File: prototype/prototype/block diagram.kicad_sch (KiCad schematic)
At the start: 30 parts, among them J1 Conn_01x06_Pin, Q2 NMOS, Q3 NMOS, Q4 NMOS, U10 AMS1117-3.3, U11 ESP32-WROOM-32E, U8 CI121S021 [adc], U9 MQ-4M

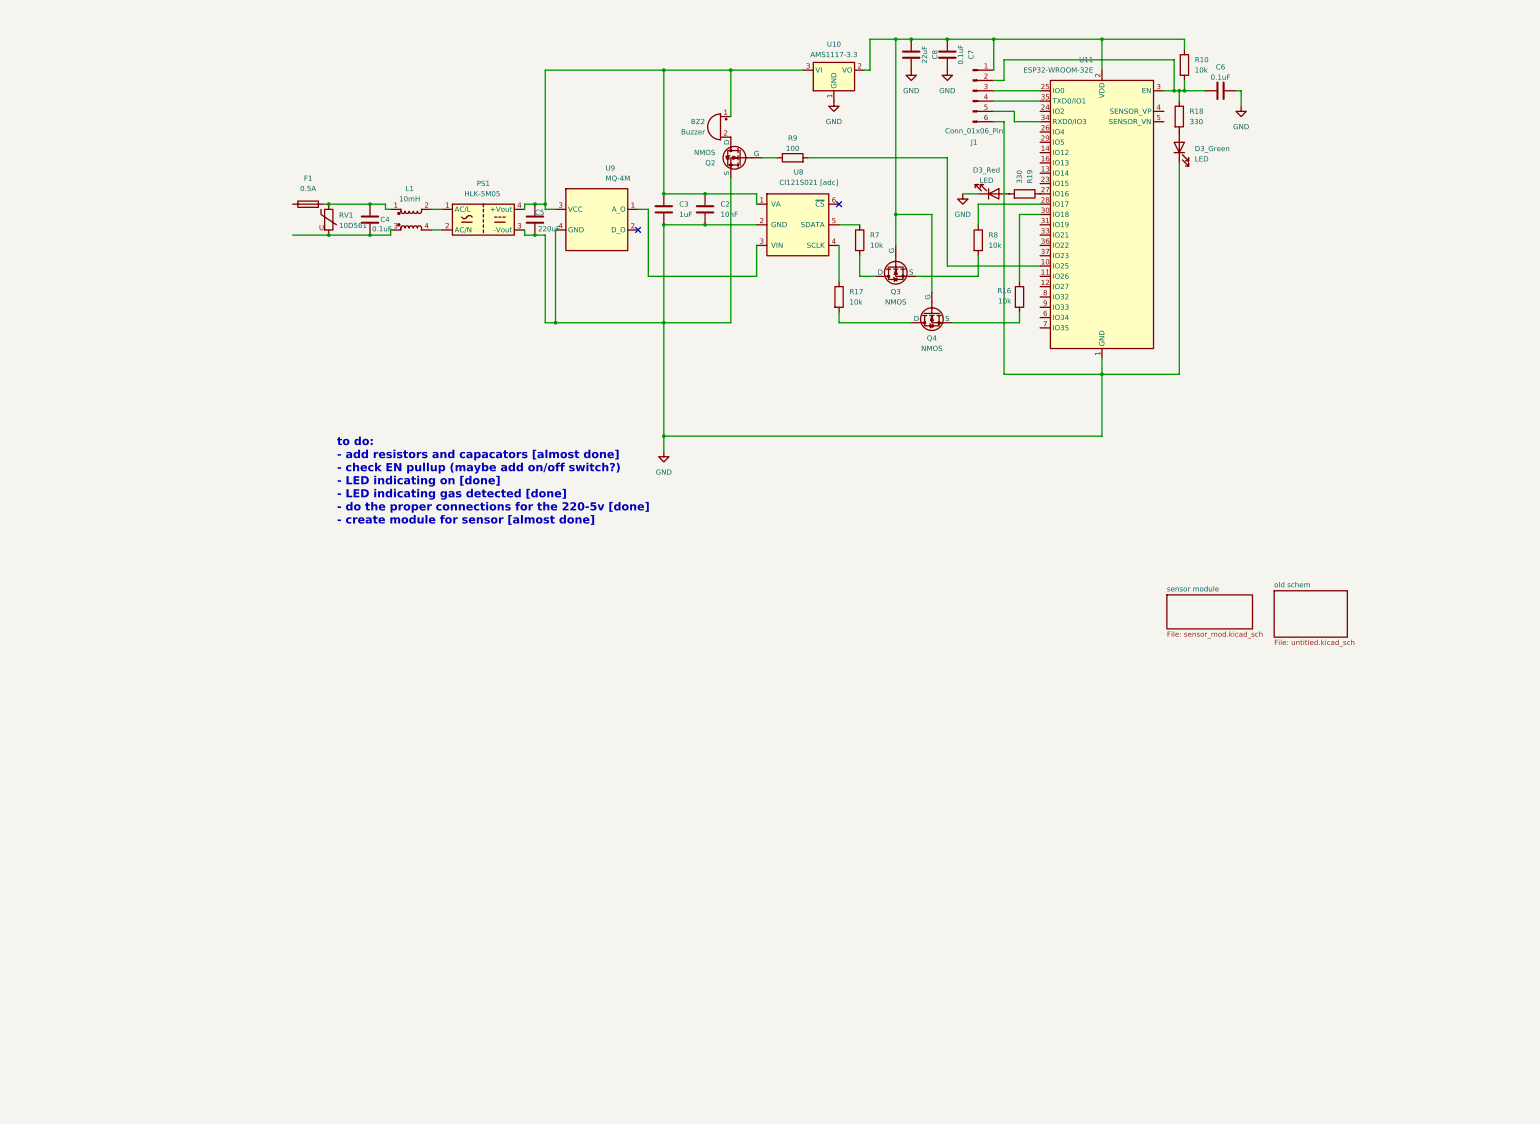
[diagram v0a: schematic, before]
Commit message: cleaning up schematic of prototype
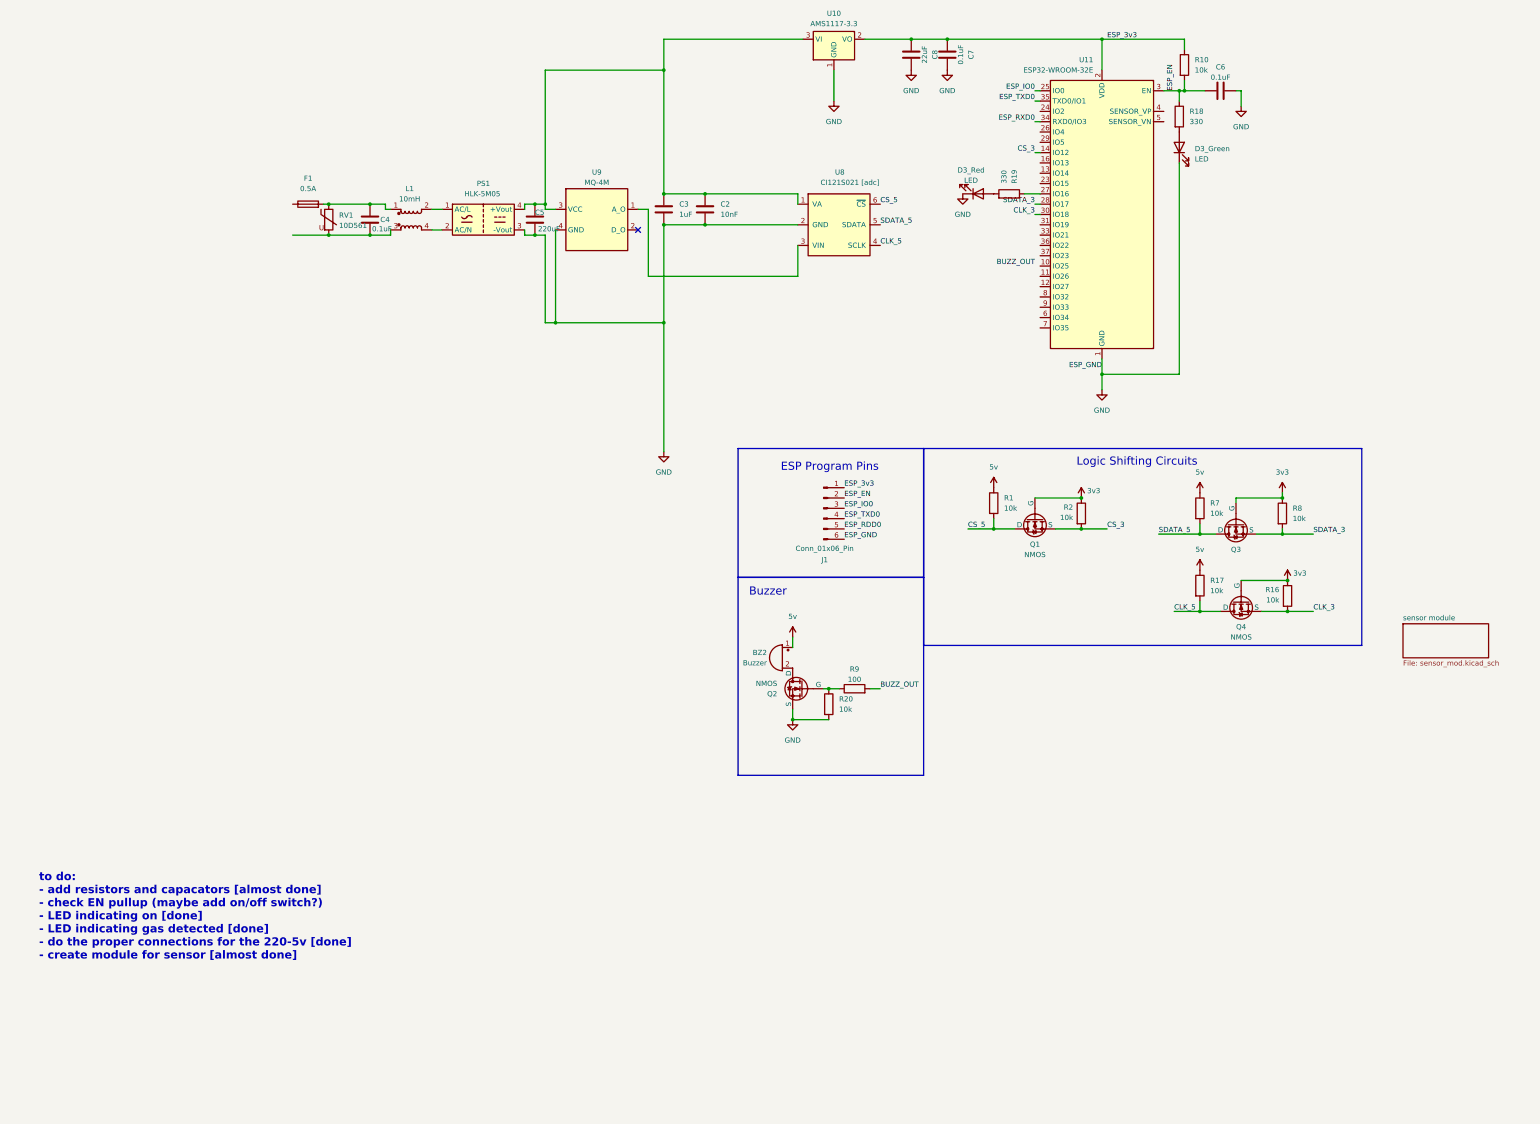
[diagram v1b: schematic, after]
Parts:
- added Q1: NMOS, symbol Simulation_SPICE:NMOS
- added R1, R2, R20: 10k, symbol Device:R
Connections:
- net GND: now also R20.2
- net 3v3: now reaches R16.1
- net 3v3: now also Q3.2 (G), Q4.2 (G), R8.1, Q1.2 (G), R2.1; no longer U11.30 (IO18)
- net CLK_3: now reaches Q4.3 (S), R16.2
- net CLK_3: now also U11.30 (IO18)
- net CLK_5: now reaches Q4.1 (D), R17.2
- net CLK_5: now also U8.4 (SCLK)
- net ESP_3v3: now reaches C7.1, C8.1, J1.1 (Pin_1), R10.1, U10.2 (VO), U11.2 (VDD)
- net ESP_3v3: no longer Q3.2 (G), Q4.2 (G)
- net at Q2.2 (G), R9.1: now also R20.1
- net at U11.10 (IO25): no longer R9.2
- net at C2.1, C3.1, C5.1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: no longer BZ2.1 (+)
- net 5v: now reaches R7.1
- net 5v: now also BZ2.1 (+), R17.1, R1.1; no longer U8.5 (SDATA)
- net SDATA_5: now reaches Q3.1 (D), R7.2
- net SDATA_5: now also U8.5 (SDATA)
- net SDATA_3: now reaches Q3.3 (S), R8.2
- net SDATA_3: now also U11.28 (IO17)
- net ESP_EN: now reaches C6.1, J1.2 (Pin_2), R10.2, R18.1, U11.3 (EN)
- net CS_5: now reaches U8.6 (~{CS})
- net CS_5: now also Q1.1 (D), R1.2
- net CS_3: now reaches U11.14 (IO12)
- net CS_3: now also Q1.3 (S), R2.2
- net ESP_IO0: now reaches J1.3 (Pin_3), U11.25 (IO0)
- net ESP_RDD0: now reaches J1.5 (Pin_5)
- net ESP_RDD0: no longer U11.34 (RXD0/IO3)
- net ESP_TXD0: now reaches J1.4 (Pin_4), U11.35 (TXD0/IO1)
- new net BUZZ_OUT: R9.2
- new net ESP_RXD0: U11.34 (RXD0/IO3)
- no-connect marks 2 -> 1
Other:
- removed sheet old schem
- note added: "Buzzer"
- note added: "ESP Program Pins"
- note added: "Logic Shifting Circuits"
- moved on the sheet: BZ2, D3_Red, J1, Q2, Q3, Q4, R16, R17, R19, R7, R8, R9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

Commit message: cleaning up schematic of prototype complete
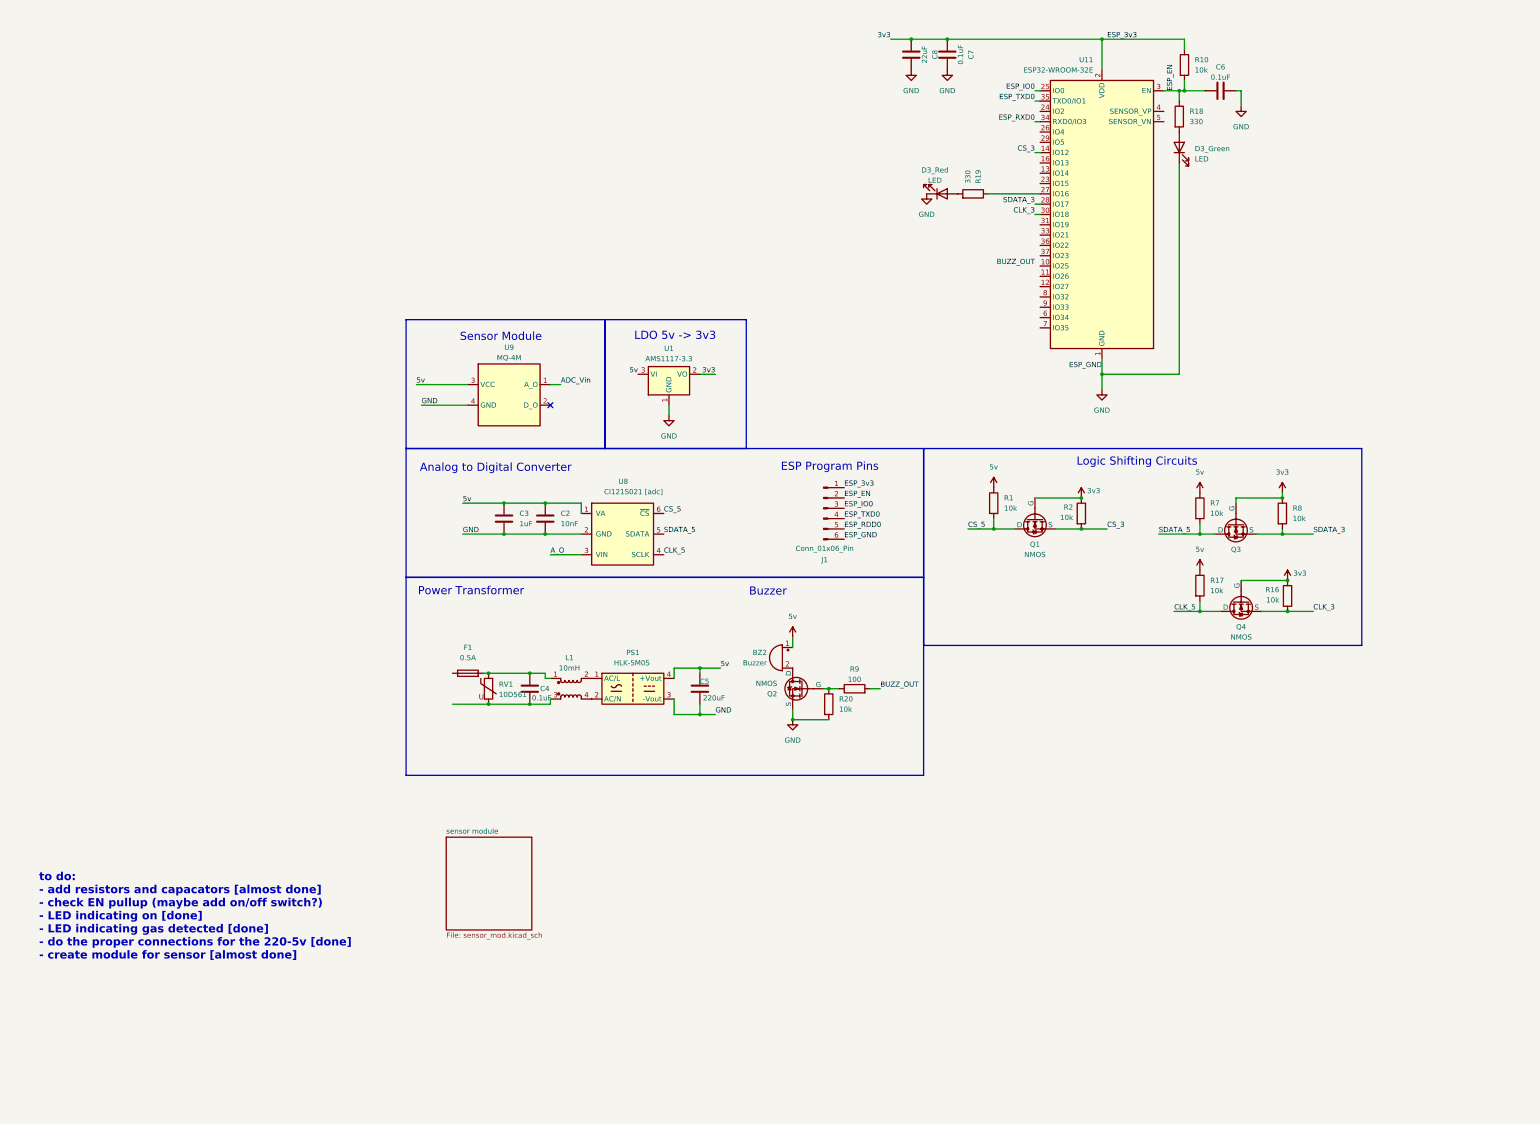
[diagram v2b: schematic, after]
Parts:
- removed U10: AMS1117-3.3, Package_TO_SOT_SMD:SOT-223-3_TabPin2, symbol Regulator_Linear:AMS1117-3.3
- added U1: AMS1117-3.3, Package_TO_SOT_SMD:SOT-223-3_TabPin2, symbol Regulator_Linear:AMS1117-3.3
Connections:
- net ESP_3v3 is gone; now on net 3v3: C7.1, C8.1, J1.1 (Pin_1), R10.1, U11.2 (VDD)
- net 3v3: now also U1.2 (VO)
- net 5v: now also C2.1, C3.1, C5.1, PS1.4 (+Vout), U8.1 (VA), U9.3 (VCC), U1.3 (VI)
- net GND: now also U1.1 (GND)
- net ADC_Vin: now reaches U9.1 (A_O)
- net ADC_Vin: no longer U8.3 (VIN)
- new net A_O: U8.3 (VIN)
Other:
- note added: "Analog to Digital Converter"
- note added: "LDO 5v -> 3v3"
- note added: "Power Transformer"
- note added: "Sensor Module"
- moved on the sheet: C2, C3, C4, C5, D3_Red, F1, L1, PS1, R19, RV1, U8, U9

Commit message: idk
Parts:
- added C10, C12: 10uF, Photon:C0603, symbol Device:C
- added R21: 1k, Photon:R_0603_1608Metric_Pad0.98x0.95mm_HandSolder, symbol Device:R
- added R23: R, symbol Device:R
- added U5: MQ-6, Sensor:MQ-6, symbol Sensor_Gas:MQ-6
- C2, C3, C4, C5, C6, C7, C8: footprint (none) -> Photon:C0603
- F1: footprint (none) -> Photon:Fuse_1206_3216Metric
- L1: footprint (none) -> Photon:L_APV_ANR5040
- R1, R10, R16, R17, R18, R19, R2, R20, R7, R8, R9: footprint (none) -> Photon:R_0603_1608Metric_Pad0.98x0.95mm_HandSolder
- RV1: footprint (none) -> Photon:RV_Disc_D7mm_W5.7mm_P5mm
- renumbered D3_Green to D3_Green1, D3_Red to D3_Red1
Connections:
- net 3v3: now also C12.1
- net 5v: now also C10.1
- net GND: now also C10.2, C12.2, R21.2
- new net: R21.1, U5.5 (VH-)
- new net +5v: R23.2, U5.2 (VH+), U5.4 (A2), U5.6 (A1)
- new net Analog_out: R23.1, U5.1 (B1), U5.3 (B2)
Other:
- moved on the sheet: C4, C5, F1, L1, PS1, RV1, U1

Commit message: final schematic organized
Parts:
- removed R21: 1k, Photon:R_0603_1608Metric_Pad0.98x0.95mm_HandSolder, symbol Device:R
- removed U9: MQ-4M, Sensor:MQ-6, symbol Sensor_Gas:MQ-6
- added C11: 10uF, Photon:C0603, symbol Device:C
- added D3: 1N4148, Diode_THT:D_DO-35_SOD27_P7.62mm_Horizontal, symbol Diode:1N4148
- C6: value 0.1uF -> 1uF
- Q1, Q3, Q4: value NMOS -> 2N7002
- Q2: value NMOS -> AO3400
- R1, R16, R17, R2, R7, R8: value 10k -> 4.7k
- R23: value R -> 20k
- U5: value MQ-6 -> MQ-5
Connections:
- net 5v is gone; now on net +5V: BZ2.1 (+), C10.1, C2.1, C3.1, C5.1, PS1.4 (+Vout), R1.1, R17.1, R7.1, U1.3 (VI), U8.1 (VA)
- net Analog_out is gone; now on net Sensor_A_O: R23.1, U5.1 (B1), U5.3 (B2)
- net GND: now also R23.2, U5.5 (VH-), C11.2; no longer D3_Green1.1 (K)
- net at BZ2.2 (-), Q2.1 (D): now also D3.2 (A)
- net IO_16_Detect: now reaches R19.1, U11.27 (IO16)
- net +5v renamed +5V
- net +5V: now also C11.1, D3.1 (K); no longer R23.2
- net 3v3 renamed +3.3V
- net A_O renamed Sensor_A_O
- no-connect marks 1 -> 0
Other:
- removed sheet sensor module
- note added: "ESP 32 WROOM"
- note added: "LDO 5v -> 3.3v"
- note removed: "LDO 5v -> 3v3"
- moved on the sheet: BZ2, C10, C12, C2, C3, C4, C5, C6, C7, C8, D3_Green1, D3_Red1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

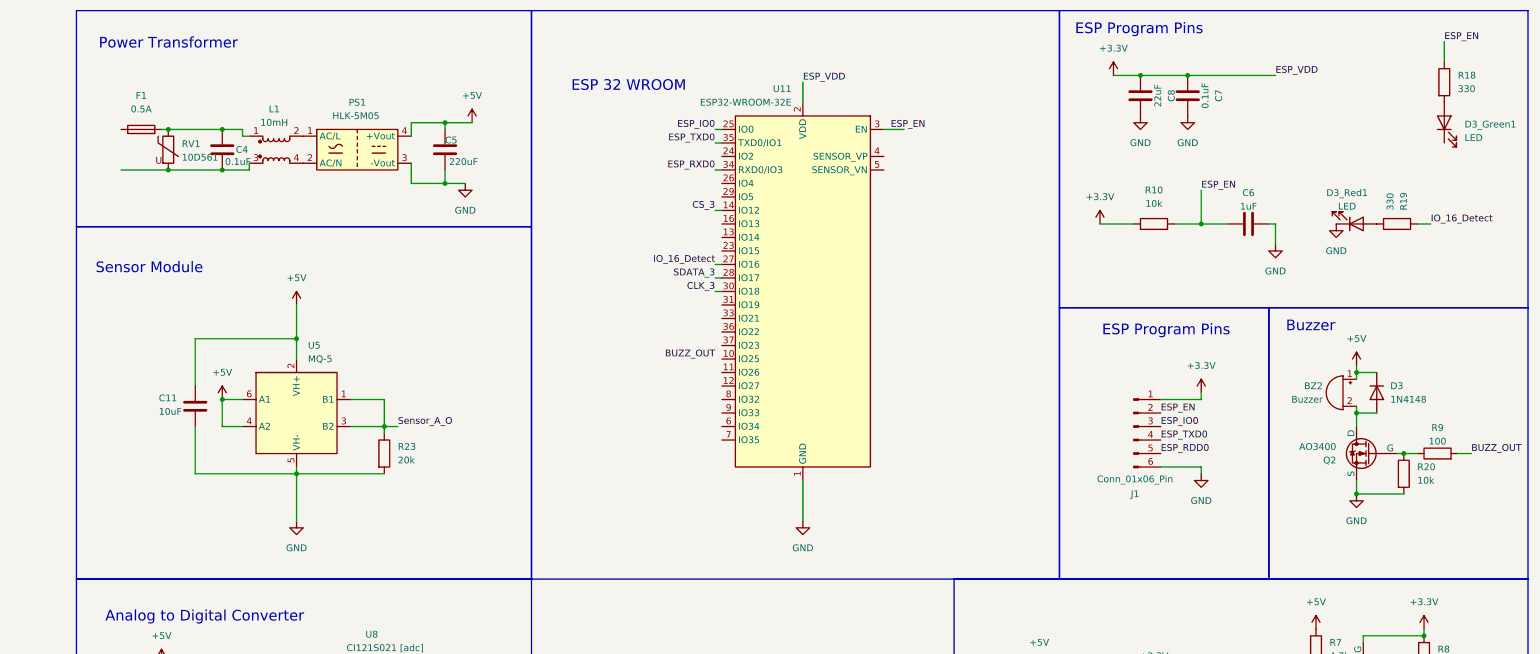
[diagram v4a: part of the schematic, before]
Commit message: updated footprints
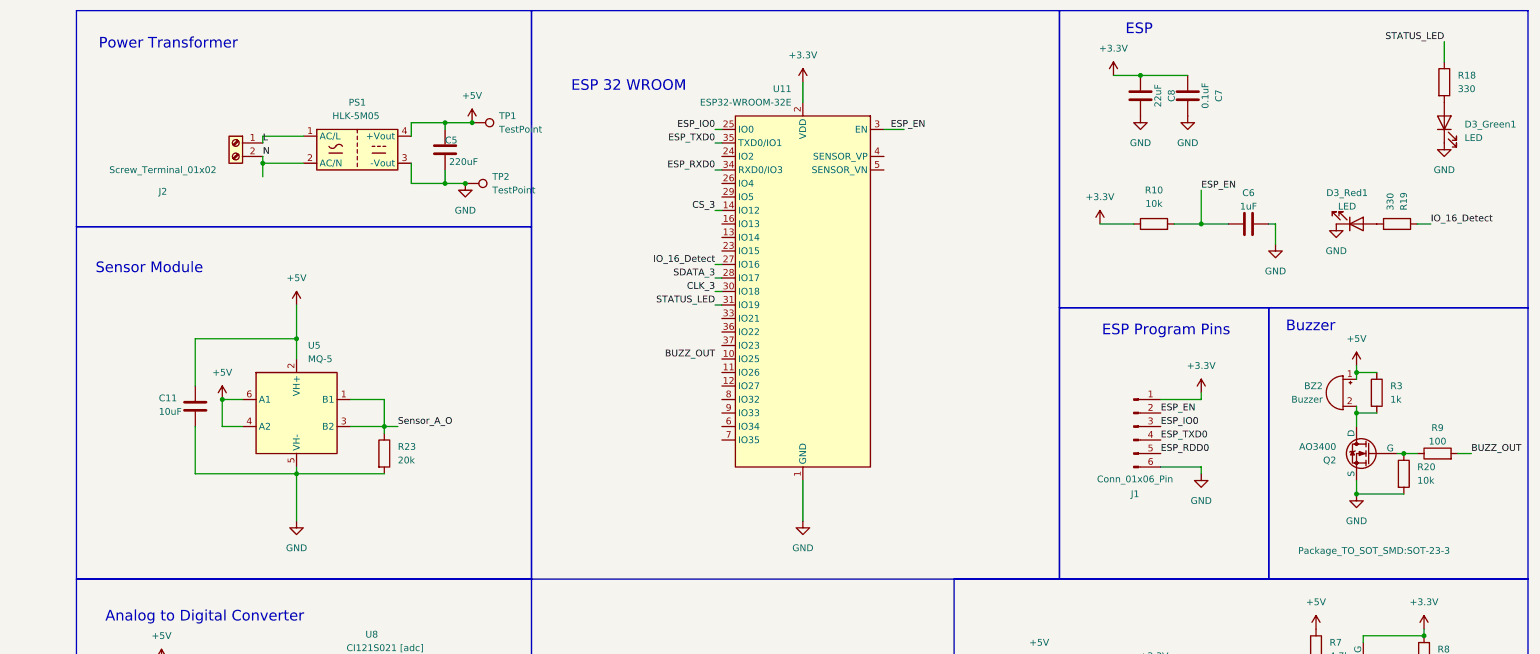
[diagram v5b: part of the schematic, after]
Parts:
- removed C4: 0.1uF, Photon:C0603, symbol Device:C
- removed D3: 1N4148, Diode_THT:D_DO-35_SOD27_P7.62mm_Horizontal, symbol Diode:1N4148
- removed F1: 0.5A, Photon:Fuse_1206_3216Metric, symbol Device:Fuse
- removed L1: 10mH, Photon:L_APV_ANR5040, symbol Device:L_Coupled
- removed RV1: 10D561, Photon:RV_Disc_D7mm_W5.7mm_P5mm, symbol Device:Varistor
- added J2: Screw_Terminal_01x02, TerminalBlock_MetzConnect:TerminalBlock_MetzConnect_Type011_RT05502HBLC_1x02_P5.00mm_Horizontal, symbol Connector:Screw_Terminal_01x02
- added R3: 1k, Photon:R_0603_1608Metric_Pad0.98x0.95mm_HandSolder, symbol Device:R
- added TP1, TP2: TestPoint, TestPoint:TestPoint_Keystone_5000-5004_Miniature, symbol Connector:TestPoint
- Q1, Q3, Q4: footprint (none) -> Photon:SOT95P240X111-3N
- Q2: footprint (none) -> Package_TO_SOT_SMD:SOT-23-3
- R23: footprint (none) -> Photon:R_0603_1608Metric_Pad0.98x0.95mm_HandSolder
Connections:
- net +5V: now also R3.1, TP1.1
- net ESP_EN: no longer R18.1
- net GND: now also D3_Green1.1 (K), TP2.1
- net at BZ2.2 (-), Q2.1 (D): now also R3.2
- net L: now reaches PS1.1 (AC/L)
- net L: now also J2.1 (Pin_1)
- net N: now reaches PS1.2 (AC/N)
- net N: now also J2.2 (Pin_2)
- net STATUS_LED: now reaches U11.31 (IO19)
- net STATUS_LED: now also R18.1
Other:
- note added: "ESP"
